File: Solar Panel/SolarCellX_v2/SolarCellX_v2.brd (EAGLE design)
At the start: 100 x 82 mm, 15 parts

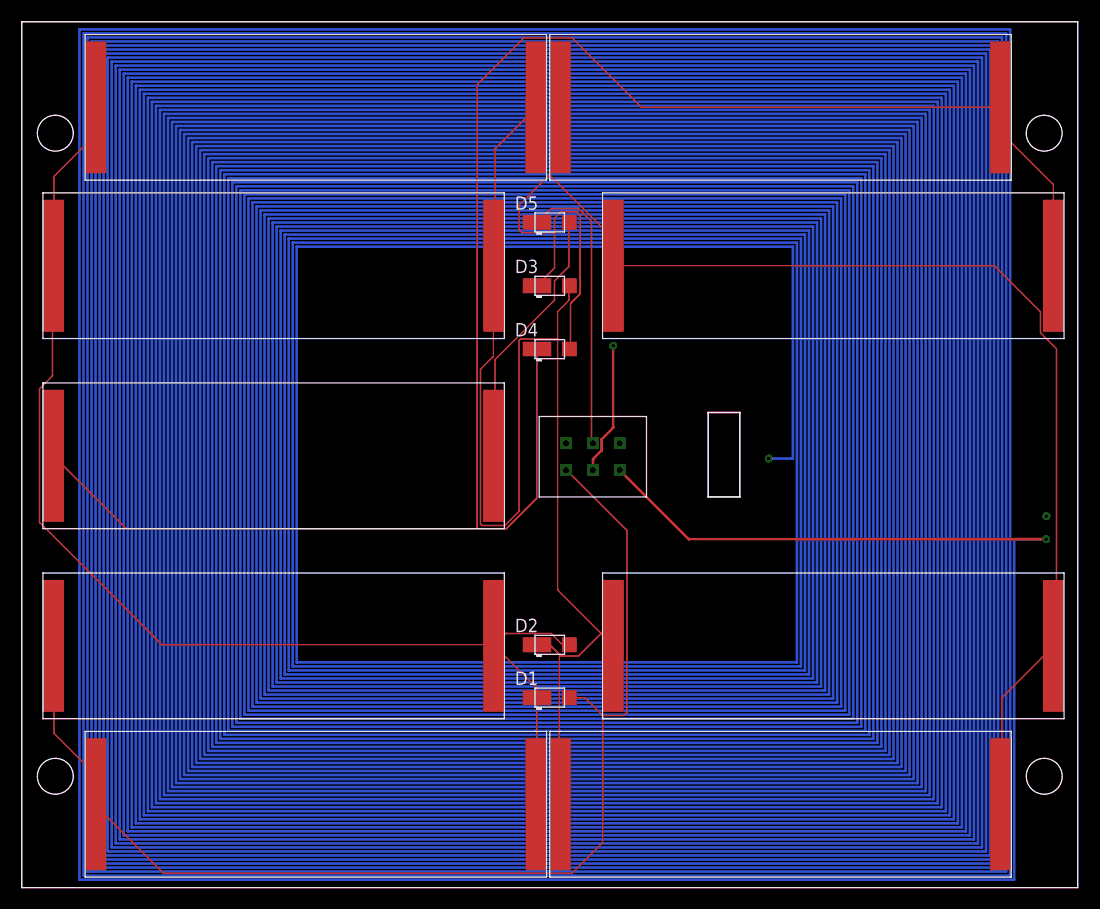
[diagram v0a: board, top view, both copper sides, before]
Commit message: Widened traces on solar board and shuffled
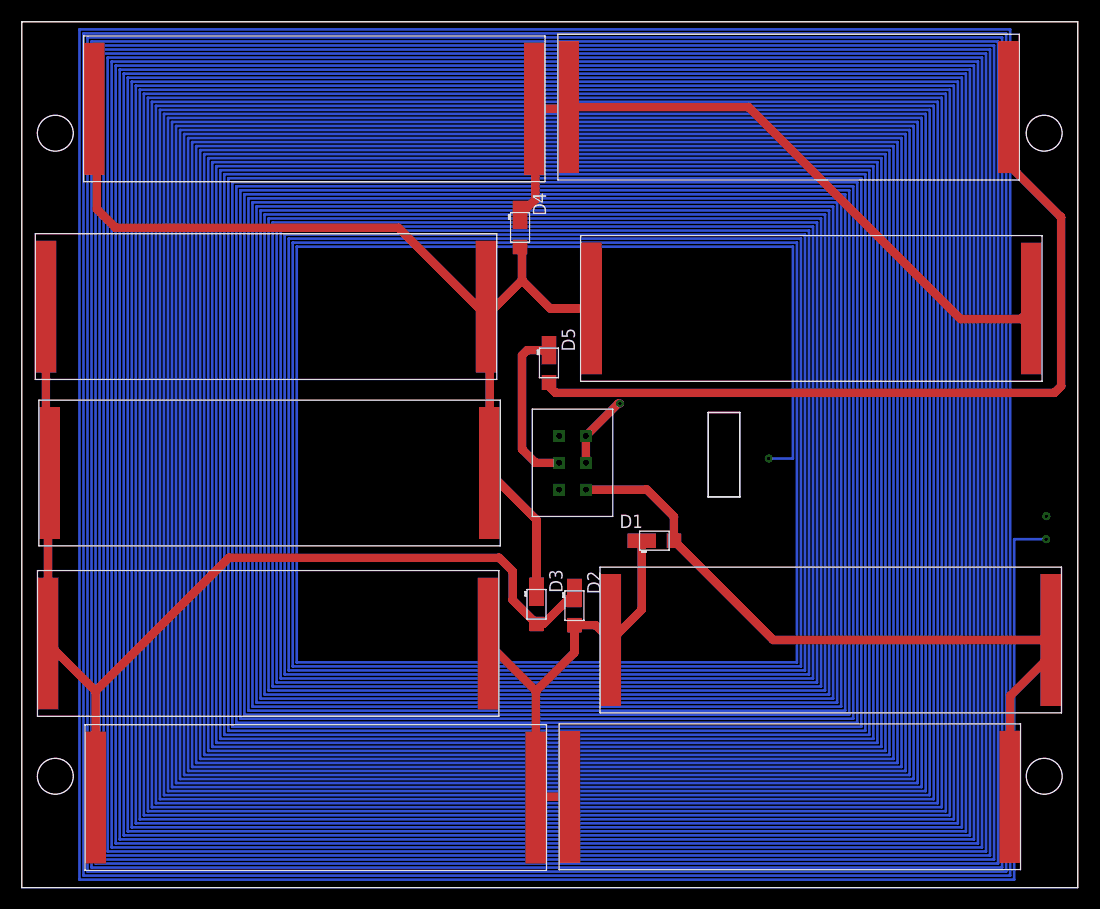
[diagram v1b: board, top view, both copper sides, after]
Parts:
- moved 12 97.5 mm to (98.5, 30.4), turned to 180 degrees
- moved 11 89.8 mm to (94.6, 15.5), turned to 180 degrees
- moved 22 62.6 mm to (1.28, 48.1)
- moved 13 60.1 mm to (49.7, 15.4), turned to 180 degrees
- moved 1 58.9 mm to (50.8, 67.0)
- moved 21 57.7 mm to (1.61, 32.4)
- moved 14 53.9 mm to (45.2, 30.0), turned to 180 degrees
- moved 23 51.3 mm to (5.85, 66.9)
- moved D3 30.2 mm to (48.7, 26.8), turned to 270 degrees
- moved 24 19.3 mm to (52.9, 48.0)
- moved D1 17.9 mm to (59.9, 32.9)
- moved D5 13.3 mm to (49.9, 49.7), turned to 270 degrees
- moved D4 11.9 mm to (47.2, 62.5), turned to 270 degrees
- moved U$1 7.20 mm to (56.0, 35.2), turned to 90 degrees
- moved D2 4.38 mm to (52.3, 26.7), turned to 270 degrees
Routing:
- net N$4: track 177.2 -> 66.8 mm
- net N$2: track 114.3 -> 42.1 mm
- net N$6: track 25.1 -> 77.9 mm
- net N$5: track 140.5 -> 95.6 mm
- net GND: track 112.4 -> 67.7 mm
- net N$1: track 42198.1 -> 42155.4 mm
- net N$3: track 124.2 -> 105.1 mm
- net V_SOLAR: track 27.3 -> 15.7 mm

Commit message: 6mil magnetorquer trace updated
Barrel jack added
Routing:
- net N$1: track 42155.4 -> 42207.4 mm
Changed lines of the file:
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@@
 <grid distance="5" unitdist="mil" unit="mil" style="lines" multiple="1" display="yes" altdistance="1" altunitdist="mm" altunit="mm"/>
 <layers>
-<layer number="1" name="Top" color="4" fill="1" visible="yes" active="yes"/>
+<layer number="1" name="Top" color="4" fill="1" visible="no" active="yes"/>
 <layer number="2" name="Route2" color="16" fill="1" visible="yes" active="yes"/>
 <layer number="3" name="Route3" color="17" fill="1" visible="no" active="no"/>
@@
 <wire x1="76.454" y1="18.288" x2="22.987" y2="18.288" width="0.254" layer="2"/>
 <wire x1="22.987" y1="18.288" x2="22.987" y2="63.754" width="0.254" layer="2"/>
-<wire x1="22.987" y1="63.754" x2="76.073" y2="63.754" width="0.254" layer="2"/>
-<wire x1="76.073" y1="63.754" x2="76.073" y2="18.288" width="0.254" layer="2"/>
+<wire x1="76.073" y1="63.754" x2="22.987" y2="63.754" width="0.254" layer="2"/>
 <wire x1="76.073" y1="18.288" x2="23.368" y2="18.288" width="0.254" layer="2"/>
-<wire x1="23.368" y1="18.288" x2="23.368" y2="63.373" width="0.254" layer="2"/>
-<wire x1="23.368" y1="63.373" x2="75.692" y2="63.373" width="0.254" layer="2"/>
+<wire x1="75.692" y1="63.373" x2="23.368" y2="63.373" width="0.254" layer="2"/>
 <wire x1="75.692" y1="63.373" x2="75.692" y2="19.05" width="0.254" layer="2"/>
 <wire x1="75.692" y1="19.05" x2="23.749" y2="19.05" width="0.254" layer="2"/>
@@
 <wire x1="53.424" y1="42.777" x2="56.494" y2="45.847" width="0.8128" layer="1"/>
 <wire x1="56.494" y1="45.847" x2="56.642" y2="45.847" width="0.8128" layer="1"/>
+<wire x1="23.368" y1="63.373" x2="23.368" y2="18.669" width="0.254" layer="2"/>
+<wire x1="23.368" y1="18.669" x2="76.073" y2="18.669" width="0.254" layer="2"/>
+<wire x1="76.073" y1="18.669" x2="76.073" y2="63.754" width="0.254" layer="2"/>
+<wire x1="76.454" y1="18.288" x2="76.073" y2="18.288" width="0" layer="19" extent="2-16"/>
 </signal>
 <signal name="N$6">
